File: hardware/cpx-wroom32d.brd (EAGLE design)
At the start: 50.8 x 50.6 mm, 39 parts, among them Q1 mmbt2222, Q2 mmbt2222, U1 ESP32-WROOM-32D, X2 ESP32_WROOM32_SKINNY

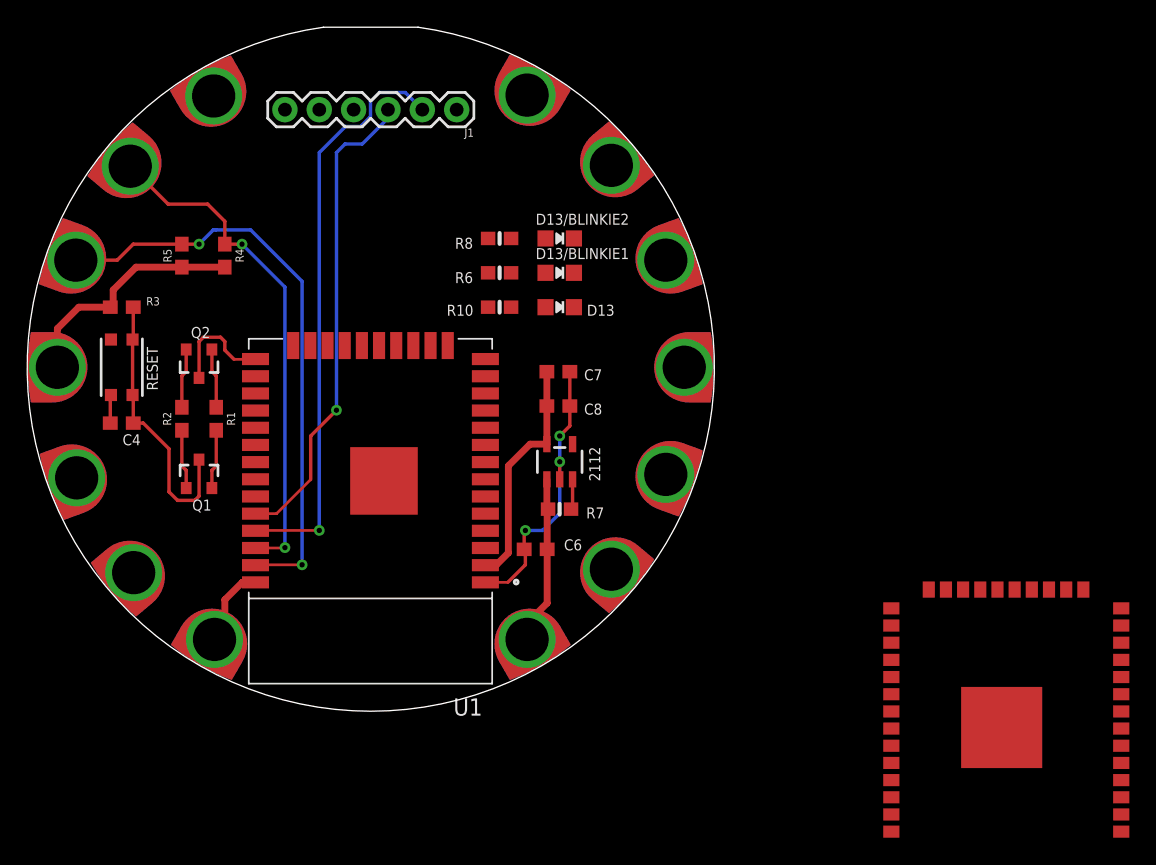
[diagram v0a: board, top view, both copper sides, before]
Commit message: About to remove some connections to the CPX.
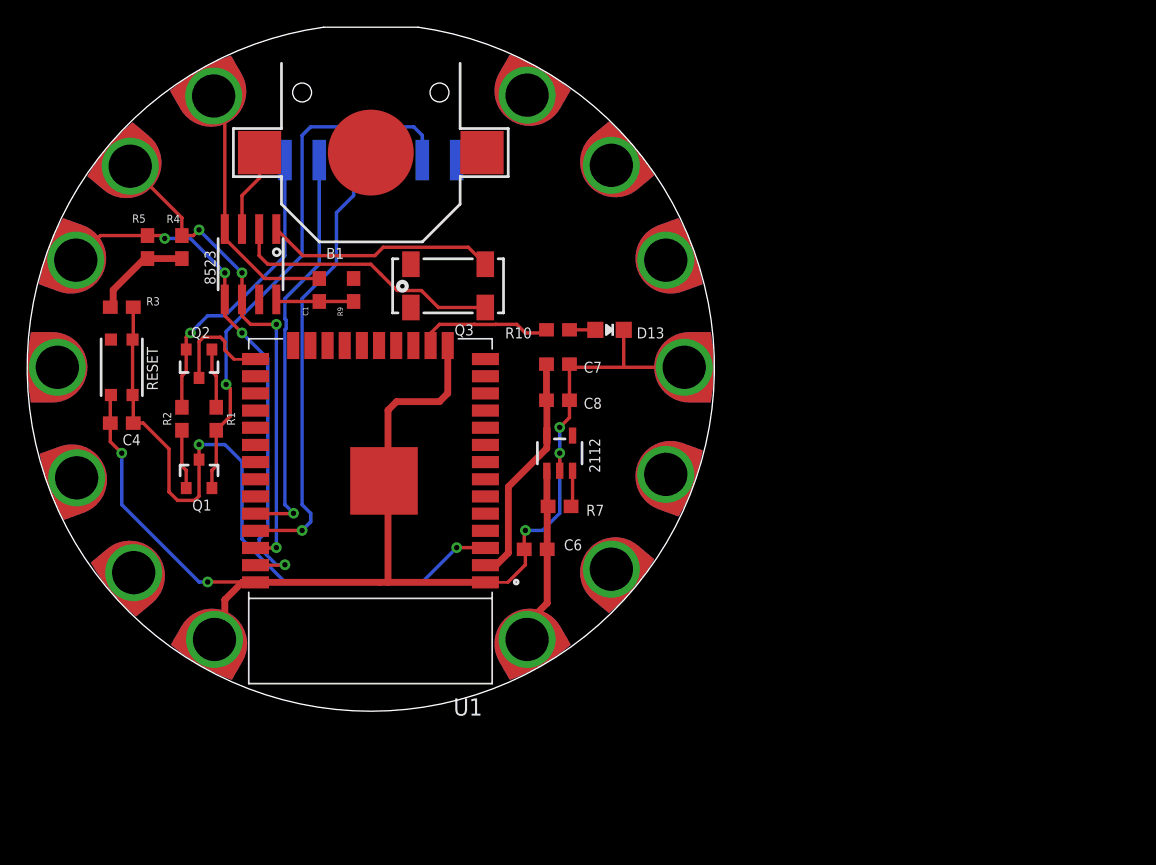
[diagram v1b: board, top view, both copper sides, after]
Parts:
- removed D13/BLINKIE1, D13/BLINKIE2: RED, microbuilder:CHIPLED_0805_NOOUTLINE
- removed R6, R8: 1K, microbuilder:0603-NO
- removed X2: ESP32_WROOM32_SKINNY, microbuilder:WROOM32_SKINNY
- added 8523: RTC_PCF8523T, microbuilder:SOIC8_150MIL
- added B1: CR1220, microbuilder:CR1220
- added C1: 10uF, SparkFun-Capacitors:0603
- added Q3: 32.768, microbuilder:CRYSTAL_8X3.8
- added R9: 1k, SparkFun-Resistors:0603
- J1: device SparkFun-Connectors:1X06 -> SparkFun-Connectors:6_PIN_SERIAL_TARGET_SIDE_RA_SMT
- moved J1 6.48 mm to (0.00, 20.3), flipped to the bottom
- moved R10 4.63 mm to (13.8, 2.77)
- moved D13 4.05 mm to (17.7, 2.77)
- moved R4 3.24 mm to (-14.0, 8.89)
- moved R5 2.62 mm to (-16.5, 8.89)
- moved 2112 0.64 mm to (14.0, -6.35)
- moved C7 0.56 mm to (13.8, 0.23)
- moved C8 0.43 mm to (13.8, -2.43)
- moved R7 0.20 mm to (14.0, -10.3)
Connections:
- removed net A0_DAC2: X2.11
- removed net A13_I35: X2.7
- removed net A1_DAC1: X2.10
- removed net A2_I34: X2.6
- removed net A3_I39: X2.5
- removed net A4_IO36: X2.4
- removed net A5_IO4: X2.26
- removed net GPIO2: X2.24
- removed net IO12_A11: X2.14
- removed net IO14_A6: X2.13
- removed net IO15_A8: X2.23
- removed net IO16: X2.27
- removed net IO17: X2.28
- removed net IO21: X2.33
- removed net IO27_A10: X2.12
- removed net IO32_A7: X2.8
- removed net IO33_A9: X2.9
- removed net MISO: X2.31
- removed net MOSI: X2.30
- removed net N$1: D13/BLINKIE1.A, R6.2
- removed net N$2: D13/BLINKIE2.A, R8.2
- removed net SCK: X2.29
- new net CLKVCC: 8523.8, C1.1, R9.2
- new net SQW: 8523.7
- new net VBAT1: 8523.3, B1.+$1
- new net XI: 8523.1, Q3.P$1
- new net XO: 8523.2, Q3.P$4
- net 3.3V: now also R9.1; no longer X2.2
- net ESP32RXI: now also J1.2; no longer J1.3, X2.34
- net ESP32TXO: now also J1.3; no longer J1.2, X2.35
- net GND: now also 8523.4, B1.-, C1.2; no longer D13/BLINKIE1.C, D13/BLINKIE2.C, X2.1, X2.15, X2.38, X2.P$1
- net GPIO0: no longer X2.25
- net LED_BUILTIN: no longer R6.1, R8.1, X2.16
- net RESET: no longer X2.3
- net SCL: now also 8523.6; no longer X2.36
- net SDA: now also 8523.5; no longer X2.37
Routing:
- net GND: track 29.7 -> 118.0 mm, vias 3 -> 5
- net RTS: track 4.40 -> 40.3 mm, vias 0 -> 1
- net RESET: track 20.5 -> 51.4 mm, vias 0 -> 2
- net XO: track 0.00 -> 20.3 mm
- net DTR: track 4.41 -> 22.2 mm, vias 0 -> 1
- net XI: track 0.00 -> 17.0 mm
- net 3.3V: track 35.1 -> 24.6 mm
- net ESP32TXO: track 43.9 -> 33.6 mm
- net LED_BUILTIN: track 0.00 -> 10.1 mm
- net VBAT1: track 0.00 -> 6.19 mm
- net CLKVCC: track 0.00 -> 5.78 mm
- net ESP32RXI: track 35.6 -> 30.3 mm
- net SDA: track 43.7 -> 39.4 mm, vias 2 -> 4
- net N$5: track 0.00 -> 1.91 mm
- net SCL: track 39.1 -> 38.2 mm, vias 2 -> 4
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
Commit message: Routed.
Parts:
- renumbered B1 to CR1220, Q3 to XTAL
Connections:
- net 3.3V: no longer 3.3VTAP.P$1, 3V3TAP2.P$1
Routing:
- net 3.3V: track 24.6 -> 87.6 mm, vias 0 -> 2
- net GND: track 118.0 -> 158.2 mm, vias 5 -> 8
- net ESP32TXO: track 33.6 -> 48.4 mm
- net ESP32RXI: track 30.3 -> 42.9 mm, vias 1 -> 3
- net LED_BUILTIN: track 10.1 -> 14.4 mm, vias 0 -> 2

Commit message: Looks goo.
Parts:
- added BME680: BME280, microbuilder:BME280
- added FRAME1: FRAME-LETTERNO_PACKAGE, SparkFun-Aesthetics:DUMMY
- R4, R5: value 4.7k -> 10K
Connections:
- new net SDO/ADR: BME680.5
- net 3.3V: now also BME680.2, BME680.6, BME680.8
- net GND: now also BME680.1, BME680.7
- net SCL: now also BME680.4
- net SDA: now also BME680.3
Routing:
- net SDA: track 39.4 -> 80.7 mm, vias 4 -> 5
- net SCL: track 38.2 -> 78.4 mm, vias 4 -> 5
- net 3.3V: track 87.6 -> 108.0 mm, vias 2 -> 5
- net GND: track 158.2 -> 170.5 mm
- net ESP32RXI: track 42.9 -> 47.0 mm
- net ESP32TXO: track 48.4 -> 49.7 mm

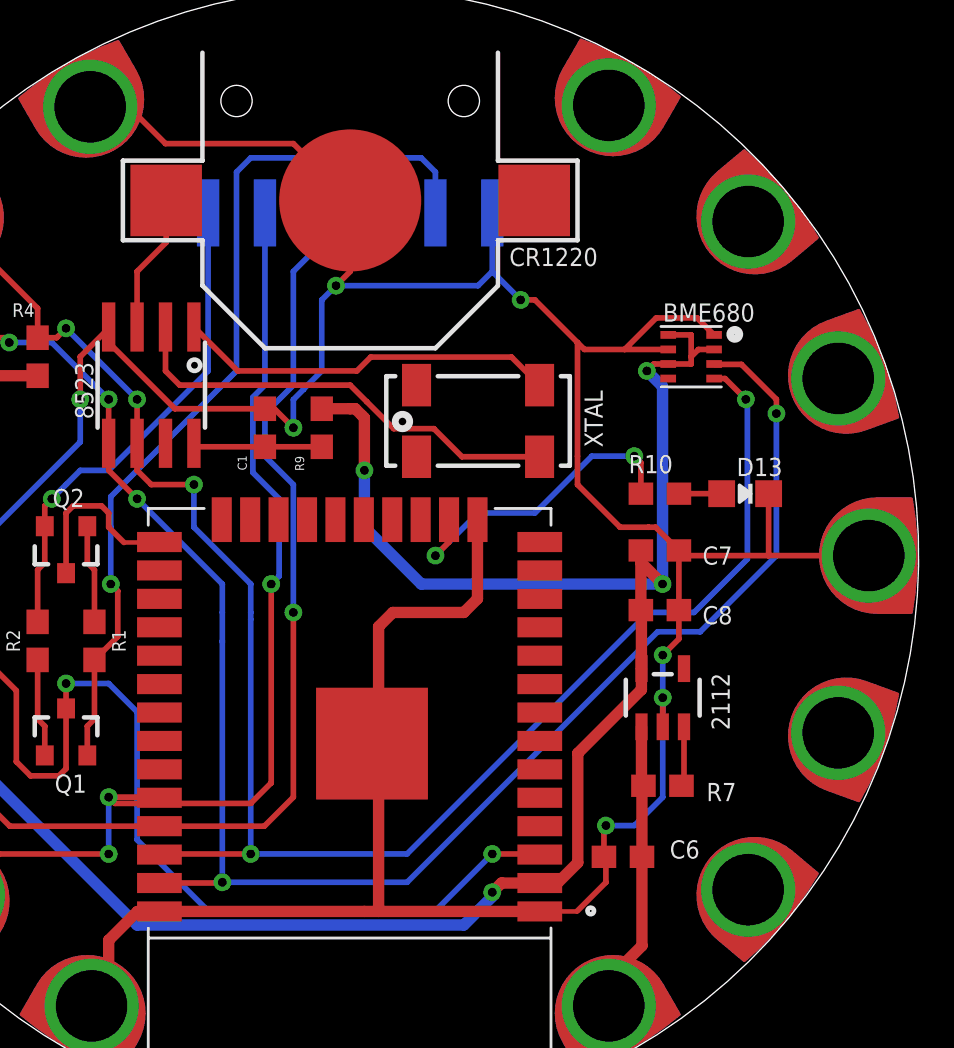
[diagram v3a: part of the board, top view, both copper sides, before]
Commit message: Cleaned up labeling, schematic.
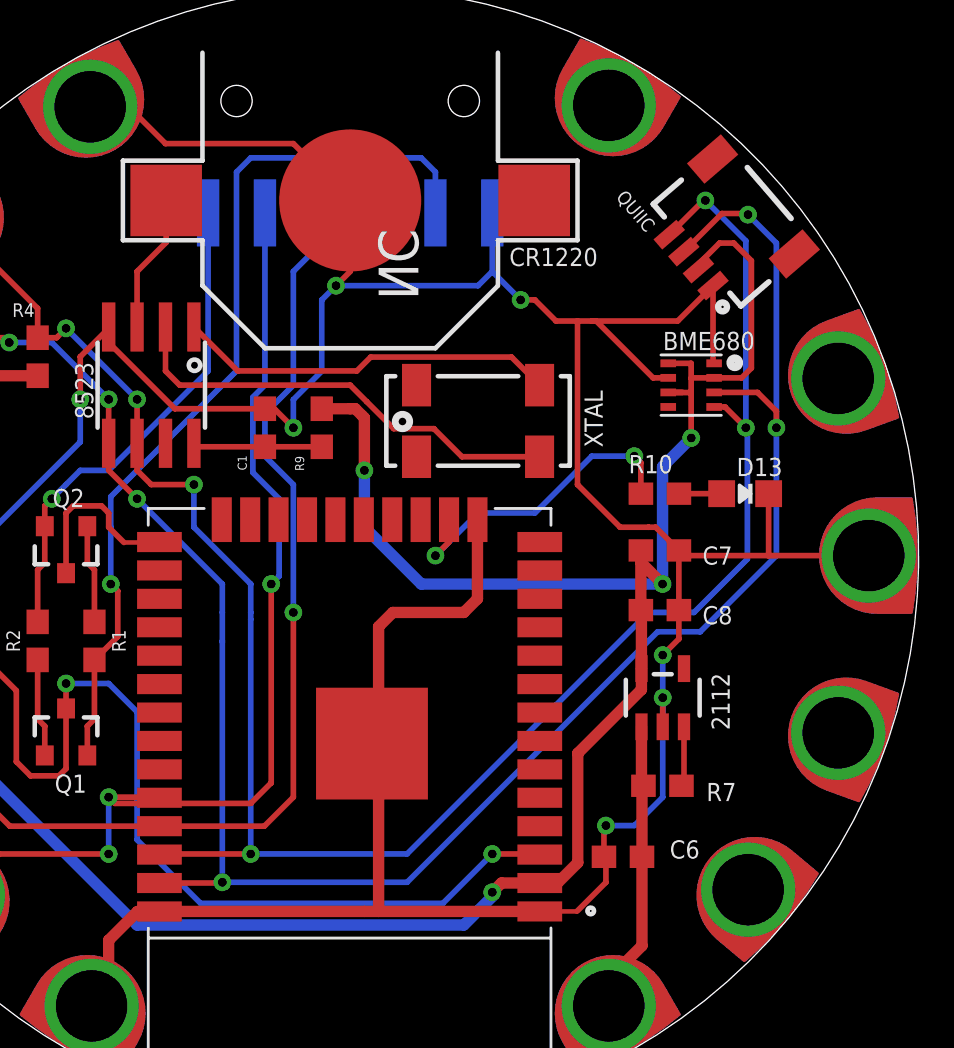
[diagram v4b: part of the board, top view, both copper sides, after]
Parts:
- removed FRAME1: FRAME-LETTERNO_PACKAGE, SparkFun-Aesthetics:DUMMY
- removed IO10: SEWTAP-ALLIGATOR, microbuilder:SEWALLI
- removed U$16: (no value), silks:CPLAY_EXPRESS_FRONT_REVG
- removed U$46: (no value), silks:CPLAY_EXPRESS_BACK_REVD
- added QUIIC: (no value), SparkFun-Connectors:1X04_1MM_RA
- moved BME680 1.27 mm to (15.2, 7.62)
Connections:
- removed net D10_A3: IO10.P$1
- net 3.3V: now also QUIIC.2
- net GND: now also QUIIC.1
- net SCL: now also QUIIC.4
- net SDA: now also QUIIC.3
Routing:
- net SDA: track 80.7 -> 93.5 mm, vias 5 -> 6
- net SCL: track 78.4 -> 90.3 mm, vias 5 -> 6
- net 3.3V: track 108.0 -> 116.6 mm
- net GND: track 170.5 -> 176.6 mm
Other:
- board text added: "DTR"
- board text added: "ESPRXI"
- board text added: "ESPTXO"
- board text added: "GND"
- board text added: "NC"
- board text added: "RTS"

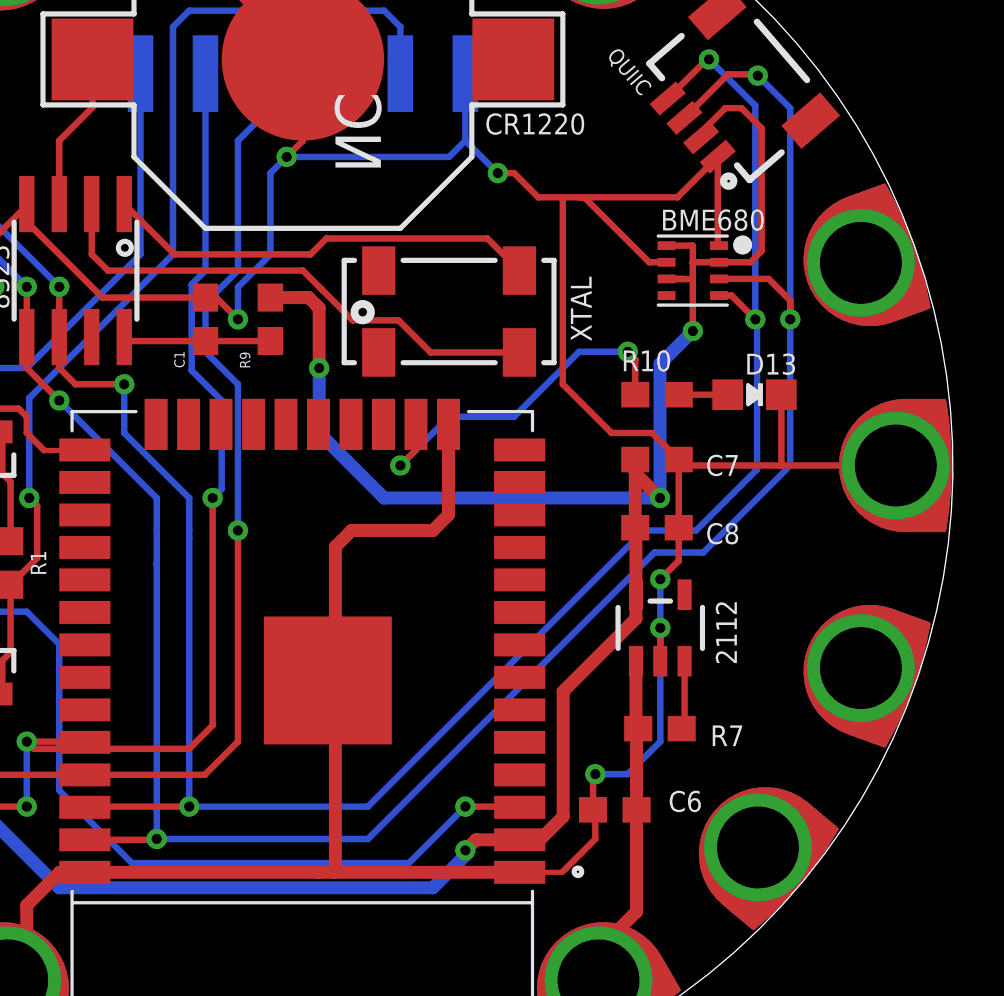
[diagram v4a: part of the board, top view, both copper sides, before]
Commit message: Forgot .gitignore, updates.
* Added a wakeup line to A2 on the CPX.
  Toggling this is to trigger the external interrupt on
  the ESP32. This seems better than playing games with RX/TX

* Moved BME680 a bit, to get it away from the QUIIC connector.

* Exploring sleep. Need to think about what I want for a serial protocol. Line-oriented? Byte-oriented?

I'd rather we were using I2C for this, but for the team, we're using Python.
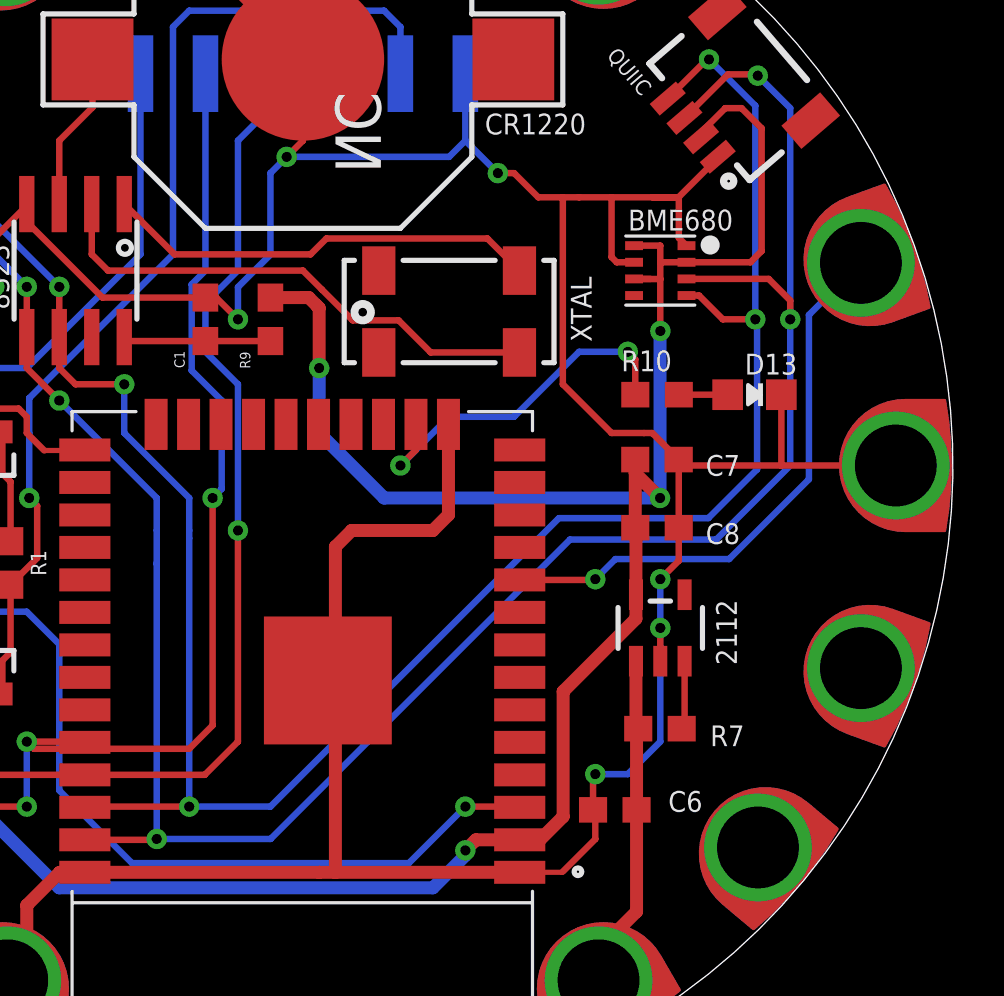
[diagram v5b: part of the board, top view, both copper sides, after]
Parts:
- moved BME680 1.27 mm to (14.0, 7.62)
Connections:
- removed net D9_A2: IO9.P$1
- new net WAKEUP: IO9.P$1, U1.10
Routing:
- net WAKEUP: track 0.00 -> 23.4 mm, vias 0 -> 1
- net GND: track 176.6 -> 175.0 mm
- net SDA: track 93.5 -> 94.7 mm
- net SCL: track 90.3 -> 91.6 mm
- net D9_A2: track 1.19 -> 0.00 mm
- net 3.3V: track 116.6 -> 117.4 mm
